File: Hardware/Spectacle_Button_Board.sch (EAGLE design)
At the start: 45 parts, among them J17 AUDIO-JACK3, J19 FTDI_DEVICE, U1 CY8C4146LQI-S422, U2 3.3V/150mA

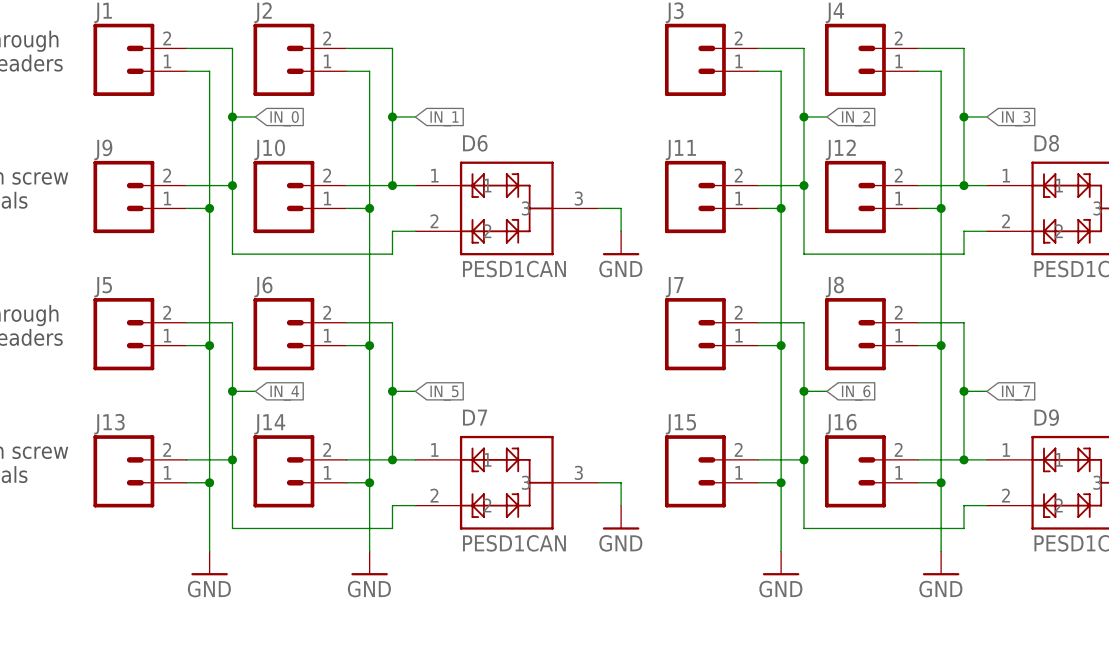
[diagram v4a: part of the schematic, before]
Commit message: Changed to pokehome connectors
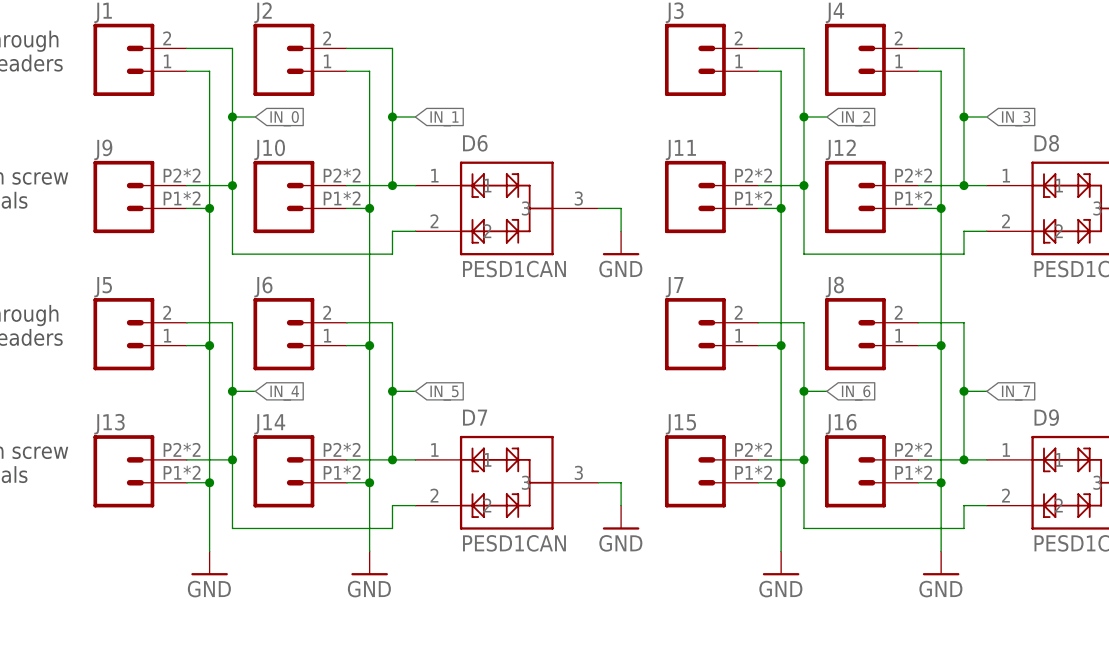
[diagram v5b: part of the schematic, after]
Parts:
- J10, J11, J12, J13, J14, J15, J16, J9: device SparkFun-Connectors:M023.5MM_LOCK -> SparkFun-Connectors:M02SMALL_POKEHOME
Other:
- moved on the sheet: J10, J11, J12, J13, J14, J15, J16, J9
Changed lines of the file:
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@@
 <layer number="255" name="routoute" color="7" fill="1" visible="yes" active="yes"/>
 </layers>
-<schematic xreflabel="%F%N/%S" xrefpart="1_/%S.%C%R">
+<schematic xreflabel="%F%N/%S" xrefpart="/%S.%C%R">
 <attributes>
 </attributes>
@@
 <part name="J7" library="SparkFun-Connectors" deviceset="M02" device="PTH"/>
 <part name="J8" library="SparkFun-Connectors" deviceset="M02" device="PTH"/>
-<part name="J9" library="SparkFun-Connectors" deviceset="M02" device="3.5MM_LOCK"/>
-<part name="J10" library="SparkFun-Connectors" deviceset="M02" device="3.5MM_LOCK"/>
-<part name="J11" library="SparkFun-Connectors" deviceset="M02" device="3.5MM_LOCK"/>
-<part name="J12" library="SparkFun-Connectors" deviceset="M02" device="3.5MM_LOCK"/>
-<part name="J13" library="SparkFun-Connectors" deviceset="M02" device="3.5MM_LOCK"/>
-<part name="J14" library="SparkFun-Connectors" deviceset="M02" device="3.5MM_LOCK"/>
-<part name="J15" library="SparkFun-Connectors" deviceset="M02" device="3.5MM_LOCK"/>
-<part name="J16" library="SparkFun-Connectors" deviceset="M02" device="3.5MM_LOCK"/>
+<part name="J9" library="SparkFun-Connectors" deviceset="M02" device="SMALL_POKEHOME"/>
+<part name="J10" library="SparkFun-Connectors" deviceset="M02" device="SMALL_POKEHOME"/>
+<part name="J11" library="SparkFun-Connectors" deviceset="M02" device="SMALL_POKEHOME"/>
+<part name="J12" library="SparkFun-Connectors" deviceset="M02" device="SMALL_POKEHOME"/>
+<part name="J13" library="SparkFun-Connectors" deviceset="M02" device="SMALL_POKEHOME"/>
+<part name="J14" library="SparkFun-Connectors" deviceset="M02" device="SMALL_POKEHOME"/>
+<part name="J15" library="SparkFun-Connectors" deviceset="M02" device="SMALL_POKEHOME"/>
+<part name="J16" library="SparkFun-Connectors" deviceset="M02" device="SMALL_POKEHOME"/>
 <part name="GND2" library="SparkFun-Aesthetics" deviceset="GND" device=""/>
 <part name="GND3" library="SparkFun-Aesthetics" deviceset="GND" device=""/>

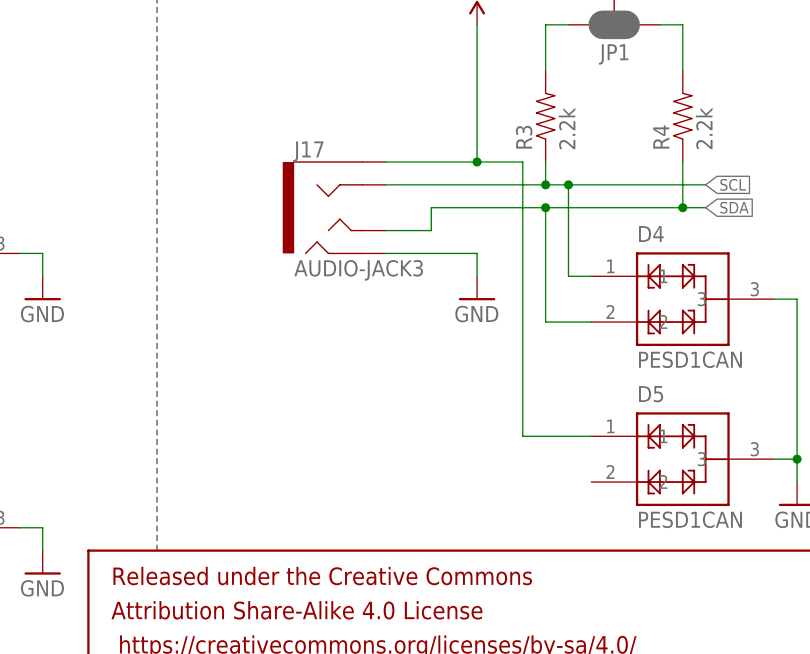
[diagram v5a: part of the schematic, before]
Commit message: Added second trrs connector
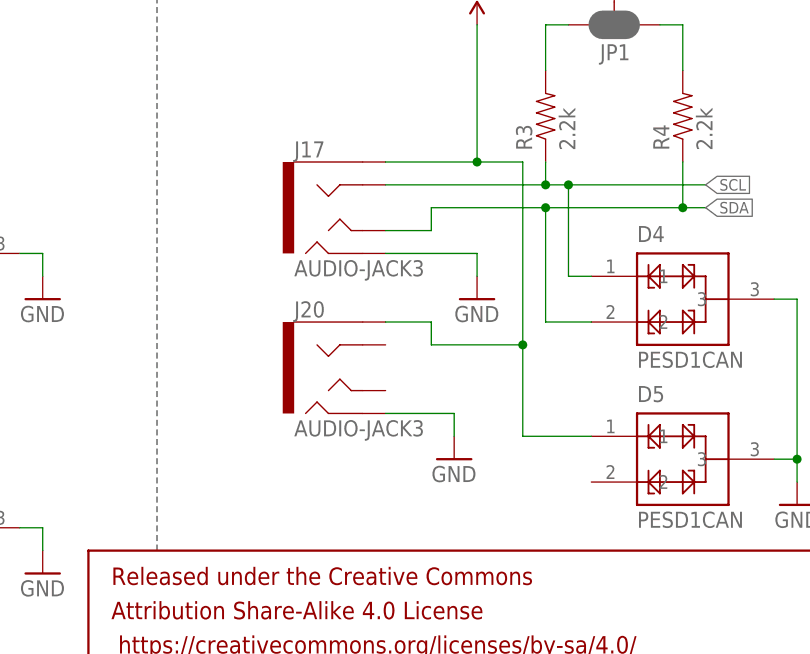
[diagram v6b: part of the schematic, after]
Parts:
- added J20: AUDIO-JACK3, SparkFun-Connectors:AUDIO-JACK3
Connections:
- net GND: now also J20.RING2
- net VIN: now also J20.EARTH
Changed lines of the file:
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@@
 <part name="SUPPLY13" library="SparkFun-Aesthetics" deviceset="3.3V" device=""/>
 <part name="SUPPLY14" library="SparkFun-Aesthetics" deviceset="3.3V" device=""/>
+<part name="J20" library="SparkFun-Connectors" deviceset="AUDIO-JACK3" device=""/>
+<part name="GND21" library="SparkFun-Aesthetics" deviceset="GND" device=""/>
 </parts>
 <sheets>
@@
 <instance part="SUPPLY13" gate="G$1" x="205.74" y="101.6"/>
 <instance part="SUPPLY14" gate="G$1" x="228.6" y="137.16"/>
+<instance part="J20" gate="G$1" x="175.26" y="55.88"/>
+<instance part="GND21" gate="1" x="187.96" y="45.72"/>
 </instances>
 <busses>
@@
 <wire x1="226.06" y1="63.5" x2="223.52" y2="63.5" width="0.1524" layer="91"/>
 </segment>
+<segment>
+<pinref part="J20" gate="G$1" pin="RING2"/>
+<pinref part="GND21" gate="1" pin="GND"/>
+<wire x1="180.34" y1="50.8" x2="187.96" y2="50.8" width="0.1524" layer="91"/>
+<wire x1="187.96" y1="50.8" x2="187.96" y2="48.26" width="0.1524" layer="91"/>
+</segment>
 </net>
 <net name="IN_0" class="0">
@@
 <wire x1="190.5" y1="78.74" x2="195.58" y2="78.74" width="0.1524" layer="91"/>
 <junction x="190.5" y="78.74"/>
-<wire x1="195.58" y1="78.74" x2="195.58" y2="48.26" width="0.1524" layer="91"/>
+<wire x1="195.58" y1="78.74" x2="195.58" y2="58.42" width="0.1524" layer="91"/>
 <pinref part="D5" gate="G$1" pin="1"/>
+<wire x1="195.58" y1="58.42" x2="195.58" y2="48.26" width="0.1524" layer="91"/>
 <wire x1="195.58" y1="48.26" x2="203.2" y2="48.26" width="0.1524" layer="91"/>
-</segment>
-</net>
+<pinref part="J20" gate="G$1" pin="EARTH"/>
+<wire x1="180.34" y1="60.96" x2="185.42" y2="60.96" width="0.1524" layer="91"/>
+<wire x1="185.42" y1="60.96" x2="185.42" y2="58.42" width="0.1524" layer="91"/>
+<wire x1="185.42" y1="58.42" x2="195.58" y2="58.42" width="0.1524" layer="91"/>
+<junction x="195.58" y="58.42"/>
+</segment>
+</net>

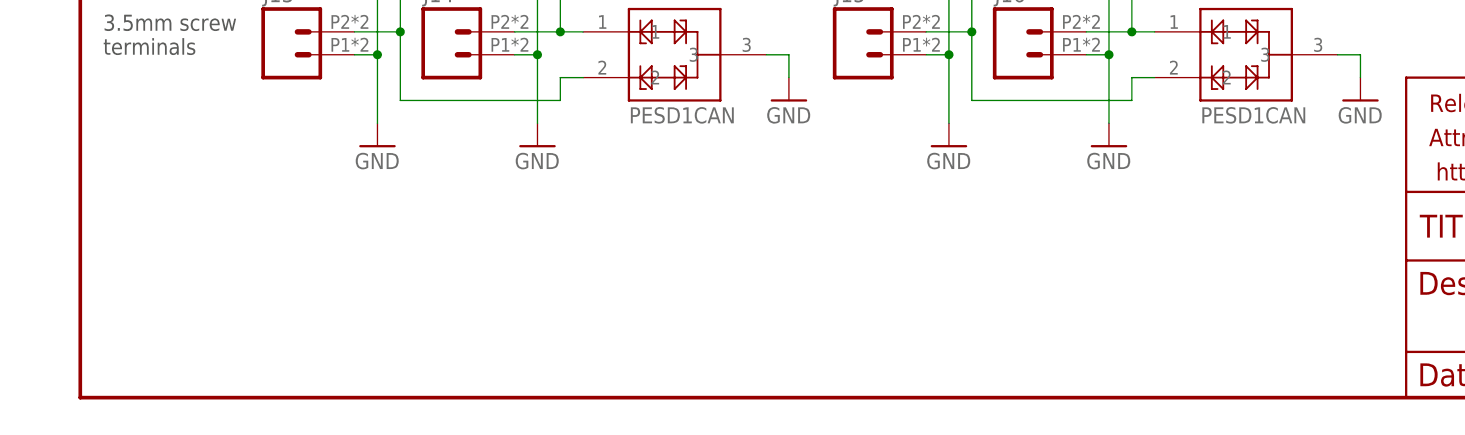
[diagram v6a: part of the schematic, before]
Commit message: added silk and dimensions
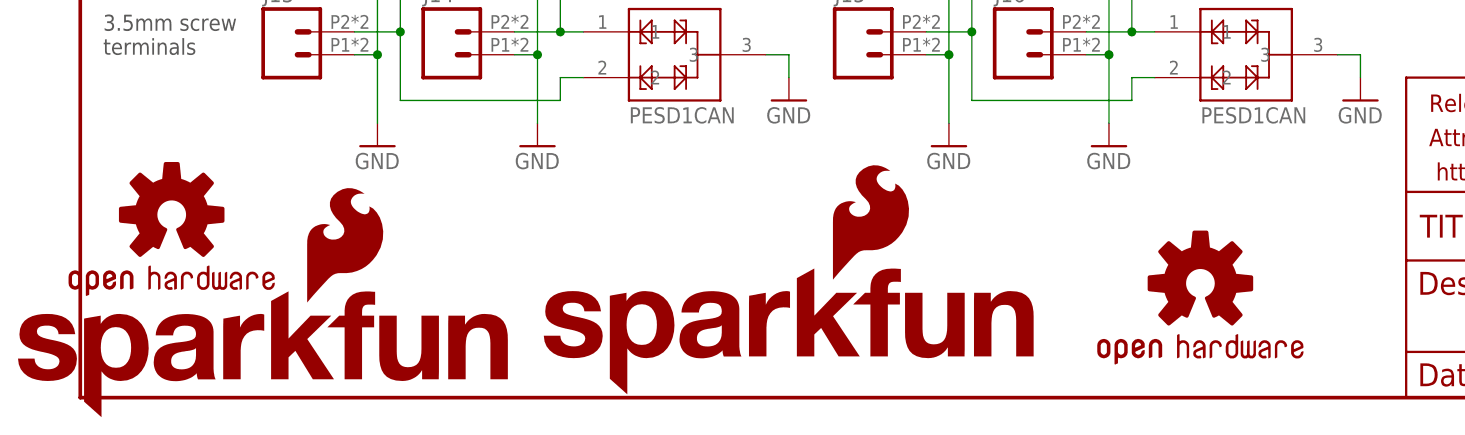
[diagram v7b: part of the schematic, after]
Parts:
- added LOGO1, LOGO4: OSHW-LOGOM, SparkFun-Aesthetics:OSHW-LOGOM
- added LOGO2, LOGO3: SFE_LOGO_NAME_FLAME.1_INCH, SparkFun-Aesthetics:SFE_LOGO_NAME_FLAME.1_INCH
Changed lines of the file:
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@@
 <part name="J20" library="SparkFun-Connectors" deviceset="AUDIO-JACK3" device=""/>
 <part name="GND21" library="SparkFun-Aesthetics" deviceset="GND" device=""/>
+<part name="LOGO1" library="SparkFun-Aesthetics" deviceset="OSHW-LOGO" device="M"/>
+<part name="LOGO2" library="SparkFun-Aesthetics" deviceset="SFE_LOGO_NAME_FLAME" device=".1_INCH"/>
+<part name="LOGO3" library="SparkFun-Aesthetics" deviceset="SFE_LOGO_NAME_FLAME" device=".1_INCH"/>
+<part name="LOGO4" library="SparkFun-Aesthetics" deviceset="OSHW-LOGO" device="M"/>
 </parts>
 <sheets>
@@
 <instance part="J20" gate="G$1" x="175.26" y="55.88"/>
 <instance part="GND21" gate="1" x="187.96" y="45.72"/>
+<instance part="LOGO1" gate="G$1" x="124.46" y="12.7"/>
+<instance part="LOGO2" gate="G$1" x="50.8" y="0"/>
+<instance part="LOGO3" gate="G$1" x="-7.62" y="-2.54"/>
+<instance part="LOGO4" gate="G$1" x="10.16" y="20.32"/>
 </instances>
 <busses>

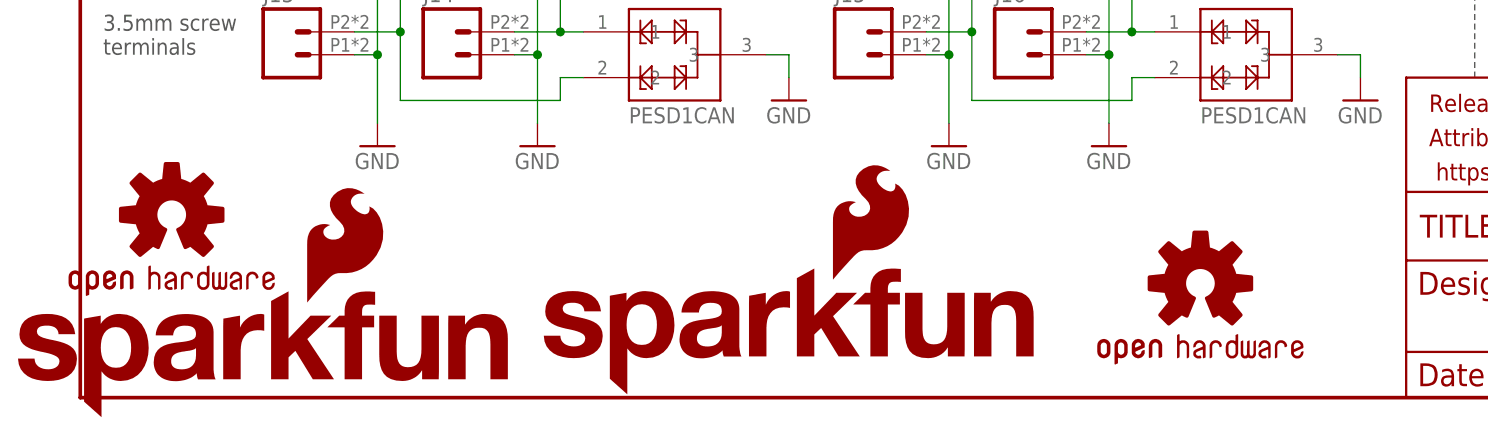
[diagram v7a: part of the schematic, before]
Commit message: Added spectacle logos
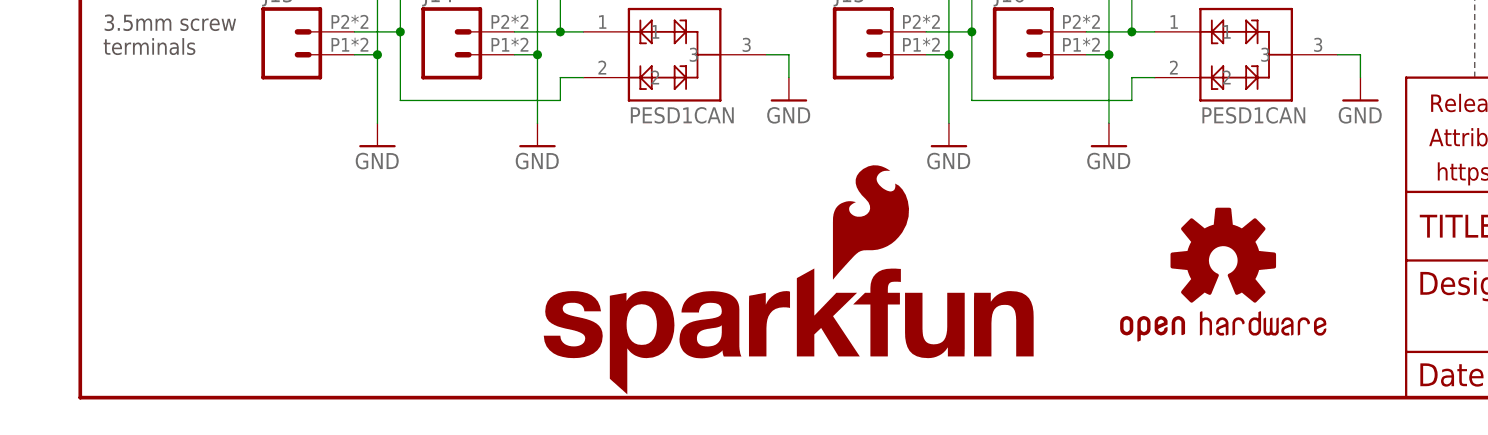
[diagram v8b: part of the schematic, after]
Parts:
- removed LOGO3: SFE_LOGO_NAME_FLAME.1_INCH, SparkFun-Aesthetics:SFE_LOGO_NAME_FLAME.1_INCH
- removed LOGO4: OSHW-LOGOM, SparkFun-Aesthetics:OSHW-LOGOM
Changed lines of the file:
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@@
 <layer number="255" name="routoute" color="7" fill="1" visible="yes" active="yes"/>
 </layers>
-<schematic xreflabel="%F%N/%S" xrefpart="/%S.%C%R">
+<schematic xreflabel="%F%N/%S" xrefpart="1_/%S.%C%R">
 <attributes>
 </attributes>
@@
 <part name="LOGO1" library="SparkFun-Aesthetics" deviceset="OSHW-LOGO" device="M"/>
 <part name="LOGO2" library="SparkFun-Aesthetics" deviceset="SFE_LOGO_NAME_FLAME" device=".1_INCH"/>
-<part name="LOGO3" library="SparkFun-Aesthetics" deviceset="SFE_LOGO_NAME_FLAME" device=".1_INCH"/>
-<part name="LOGO4" library="SparkFun-Aesthetics" deviceset="OSHW-LOGO" device="M"/>
 </parts>
 <sheets>
@@
 <instance part="J20" gate="G$1" x="175.26" y="55.88"/>
 <instance part="GND21" gate="1" x="187.96" y="45.72"/>
-<instance part="LOGO1" gate="G$1" x="124.46" y="12.7"/>
+<instance part="LOGO1" gate="G$1" x="127" y="15.24"/>
 <instance part="LOGO2" gate="G$1" x="50.8" y="0"/>
-<instance part="LOGO3" gate="G$1" x="-7.62" y="-2.54"/>
-<instance part="LOGO4" gate="G$1" x="10.16" y="20.32"/>
 </instances>
 <busses>
